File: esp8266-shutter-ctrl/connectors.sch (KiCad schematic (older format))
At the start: 7 parts, among them J1 Conn_01x08_Male, J2 Conn_01x08_Male, J3 Conn_01x04_Male, J4 Conn_01x02_Male, J5 Conn_01x04_Male, J6 Conn_01x02_Male, J7 Conn_01x04_Male

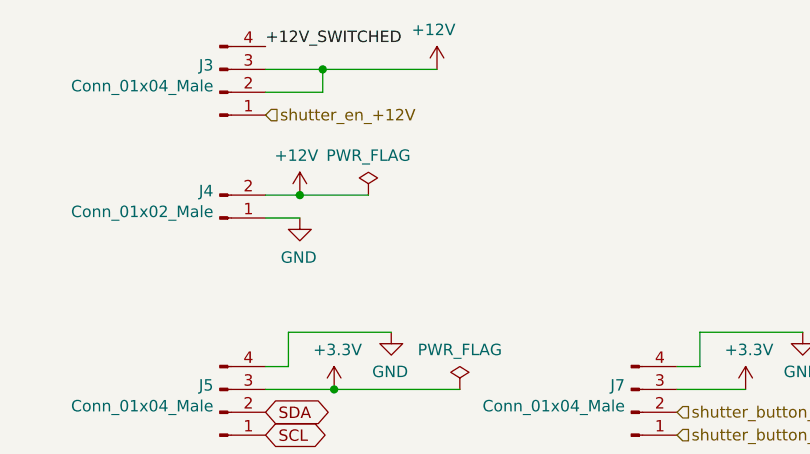
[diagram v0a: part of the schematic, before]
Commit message: shutter-ctrl: sch: added fuse and updated description
Signed-off-by: Dominik Laton <dominik.laton@web.de>
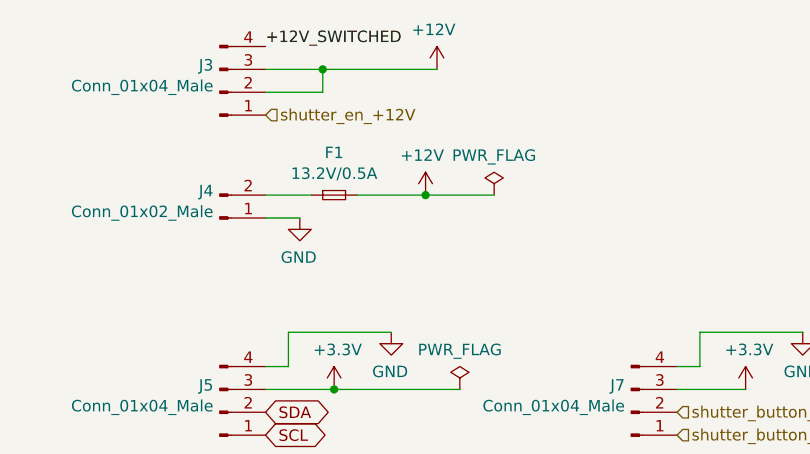
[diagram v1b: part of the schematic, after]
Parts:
- added F1: 13.2V/0.5A, Resistor_SMD:R_1206_3216Metric_Pad1.30x1.75mm_HandSolder, symbol Device:Fuse_Small
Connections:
- net +12V: now also F1.2; no longer J4.2 (Pin_2)
- new net: F1.1, J4.2 (Pin_2)
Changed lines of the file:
@@
 	-1   0    0    -1
 $EndComp
-Wire Wire Line
-	3900 1400 3750 1400
-Connection ~ 3900 1400
-Wire Wire Line
-	4200 1400 3900 1400
+Connection ~ 4450 1400
+Wire Wire Line
+	4750 1400 4450 1400
 $Comp
 L power:PWR_FLAG #FLG01
 U 1 1 601B6C0E
-P 4200 1400
-F 0 "#FLG01" H 4200 1475 50  0001 C CNN
-F 1 "PWR_FLAG" H 4200 1573 50  0000 C CNN
-F 2 "" H 4200 1400 50  0001 C CNN
-F 3 "~" H 4200 1400 50  0001 C CNN
-	1    4200 1400
+P 4750 1400
+F 0 "#FLG01" H 4750 1475 50  0001 C CNN
+F 1 "PWR_FLAG" H 4750 1573 50  0000 C CNN
+F 2 "" H 4750 1400 50  0001 C CNN
+F 3 "~" H 4750 1400 50  0001 C CNN
+	1    4750 1400
 	-1   0    0    -1
 $EndComp
@@
 L power:+12V #PWR011
 U 1 1 601B5758
-P 3900 1400
-F 0 "#PWR011" H 3900 1250 50  0001 C CNN
-F 1 "+12V" H 3915 1573 50  0000 C CNN
-F 2 "" H 3900 1400 50  0001 C CNN
-F 3 "" H 3900 1400 50  0001 C CNN
-	1    3900 1400
+P 4450 1400
+F 0 "#PWR011" H 4450 1250 50  0001 C CNN
+F 1 "+12V" H 4465 1573 50  0000 C CNN
+F 2 "" H 4450 1400 50  0001 C CNN
+F 3 "" H 4450 1400 50  0001 C CNN
+	1    4450 1400
 	-1   0    0    -1
 $EndComp
@@
 Text HLabel 5550 2450 2    50   Input ~ 0
 shutter_button_int_b
+$Comp
+L Device:Fuse_Small F1
+U 1 1 5FCCA8C7
+P 4050 1400
+F 0 "F1" H 4050 1585 50  0000 C CNN
+F 1 "13.2V/0.5A" H 4050 1494 50  0000 C CNN
+F 2 "Resistor_SMD:R_1206_3216Metric_Pad1.30x1.75mm_HandSolder" H 4050 1400 50  0001 C CNN
+F 3 "~" H 4050 1400 50  0001 C CNN
+	1    4050 1400
+	1    0    0    -1
+$EndComp
+Wire Wire Line
+	3750 1400 3950 1400
+Wire Wire Line
+	4150 1400 4450 1400
 $EndSCHEMATC
